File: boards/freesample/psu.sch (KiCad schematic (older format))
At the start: 117 parts, among them U26 MCP1755ST-5002E/MC, U27 LM27761, U28 ADP1763, U29 ADP1763, U30 OKL-T/3-W12P-C, U31 ADP1741, U32 OKL-T/3-W12P-C, U33 ADP1741, U34 ADP1741, U35 OKL-T/3-W12P-C, U36 OKL-T/3-W12P-C, U37 LM27761, U38 OKL-T/3-W12P-C, U39 LM27761, U42 ADP1741, U43 ADP1741

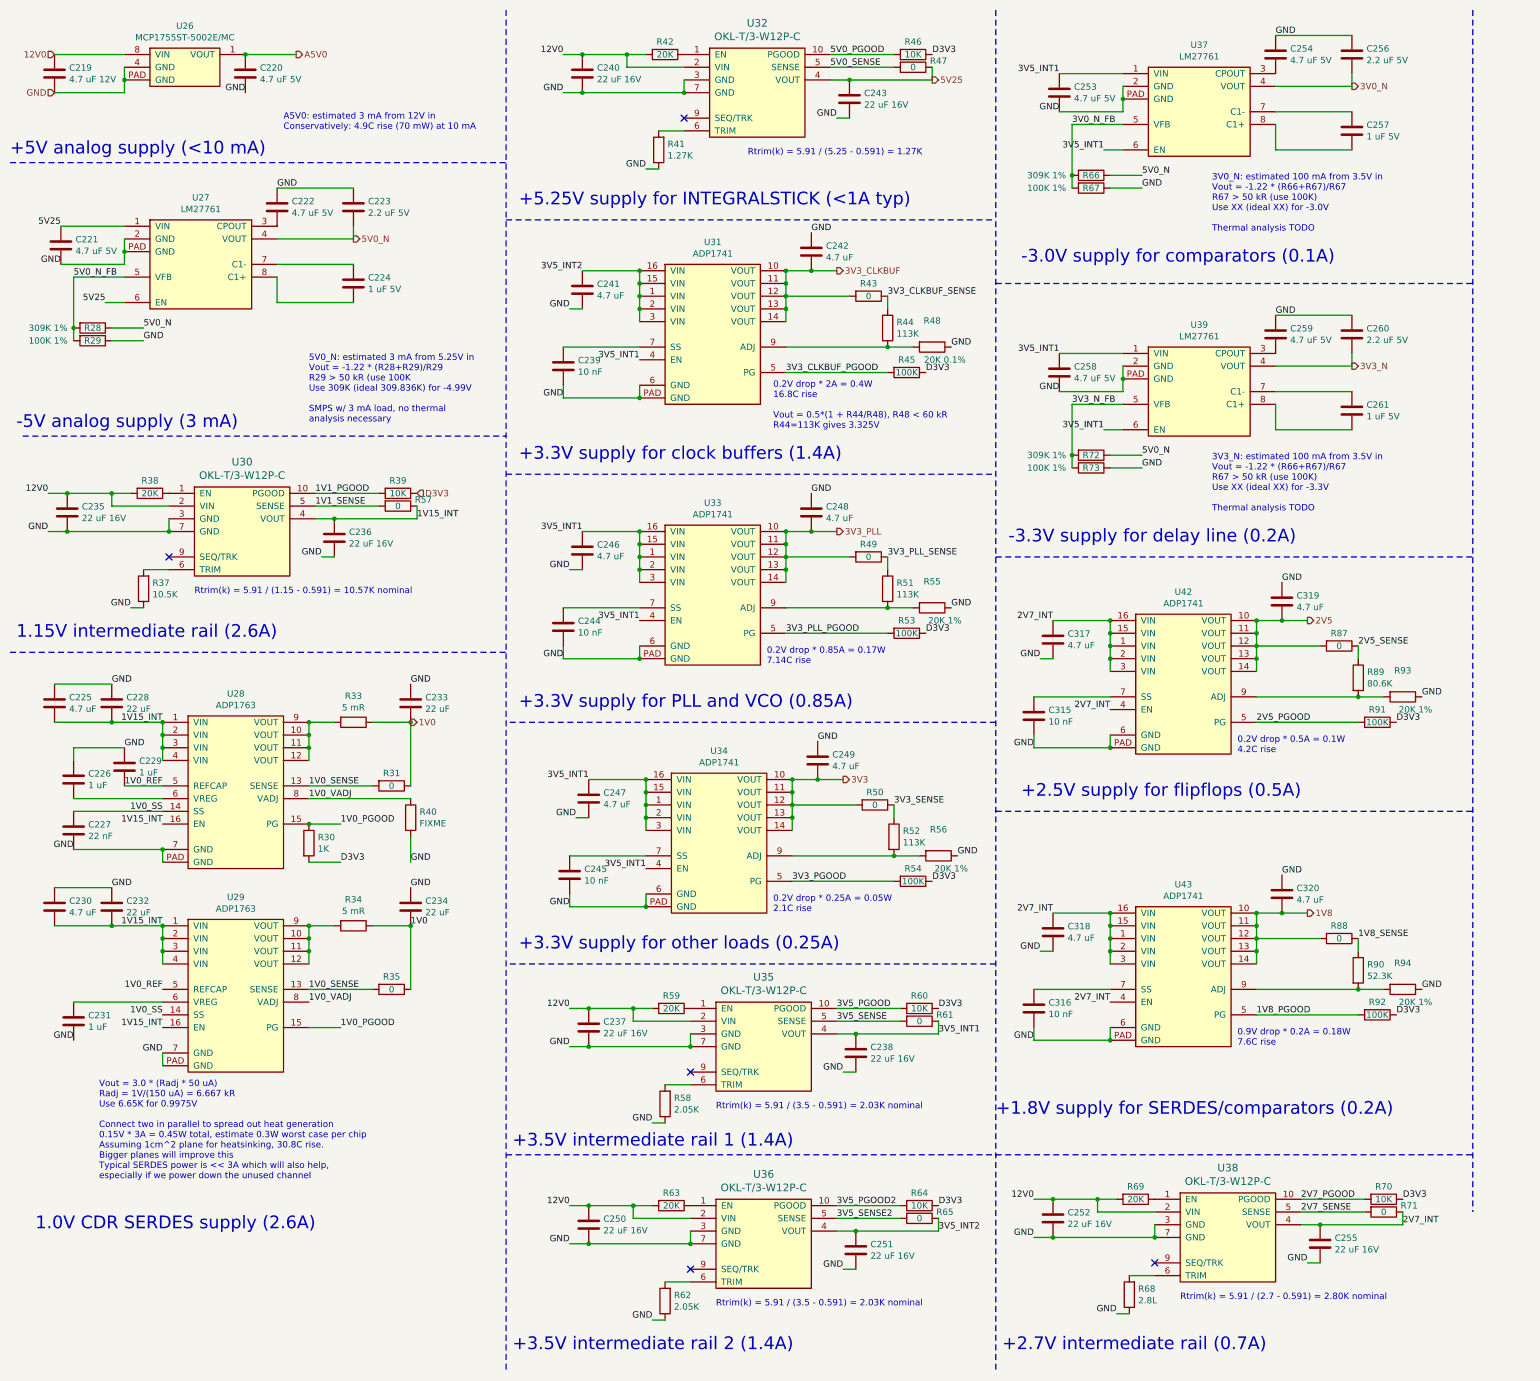
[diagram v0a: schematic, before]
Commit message: Added more test points. Started picking packages for passives. Continued schematic review.
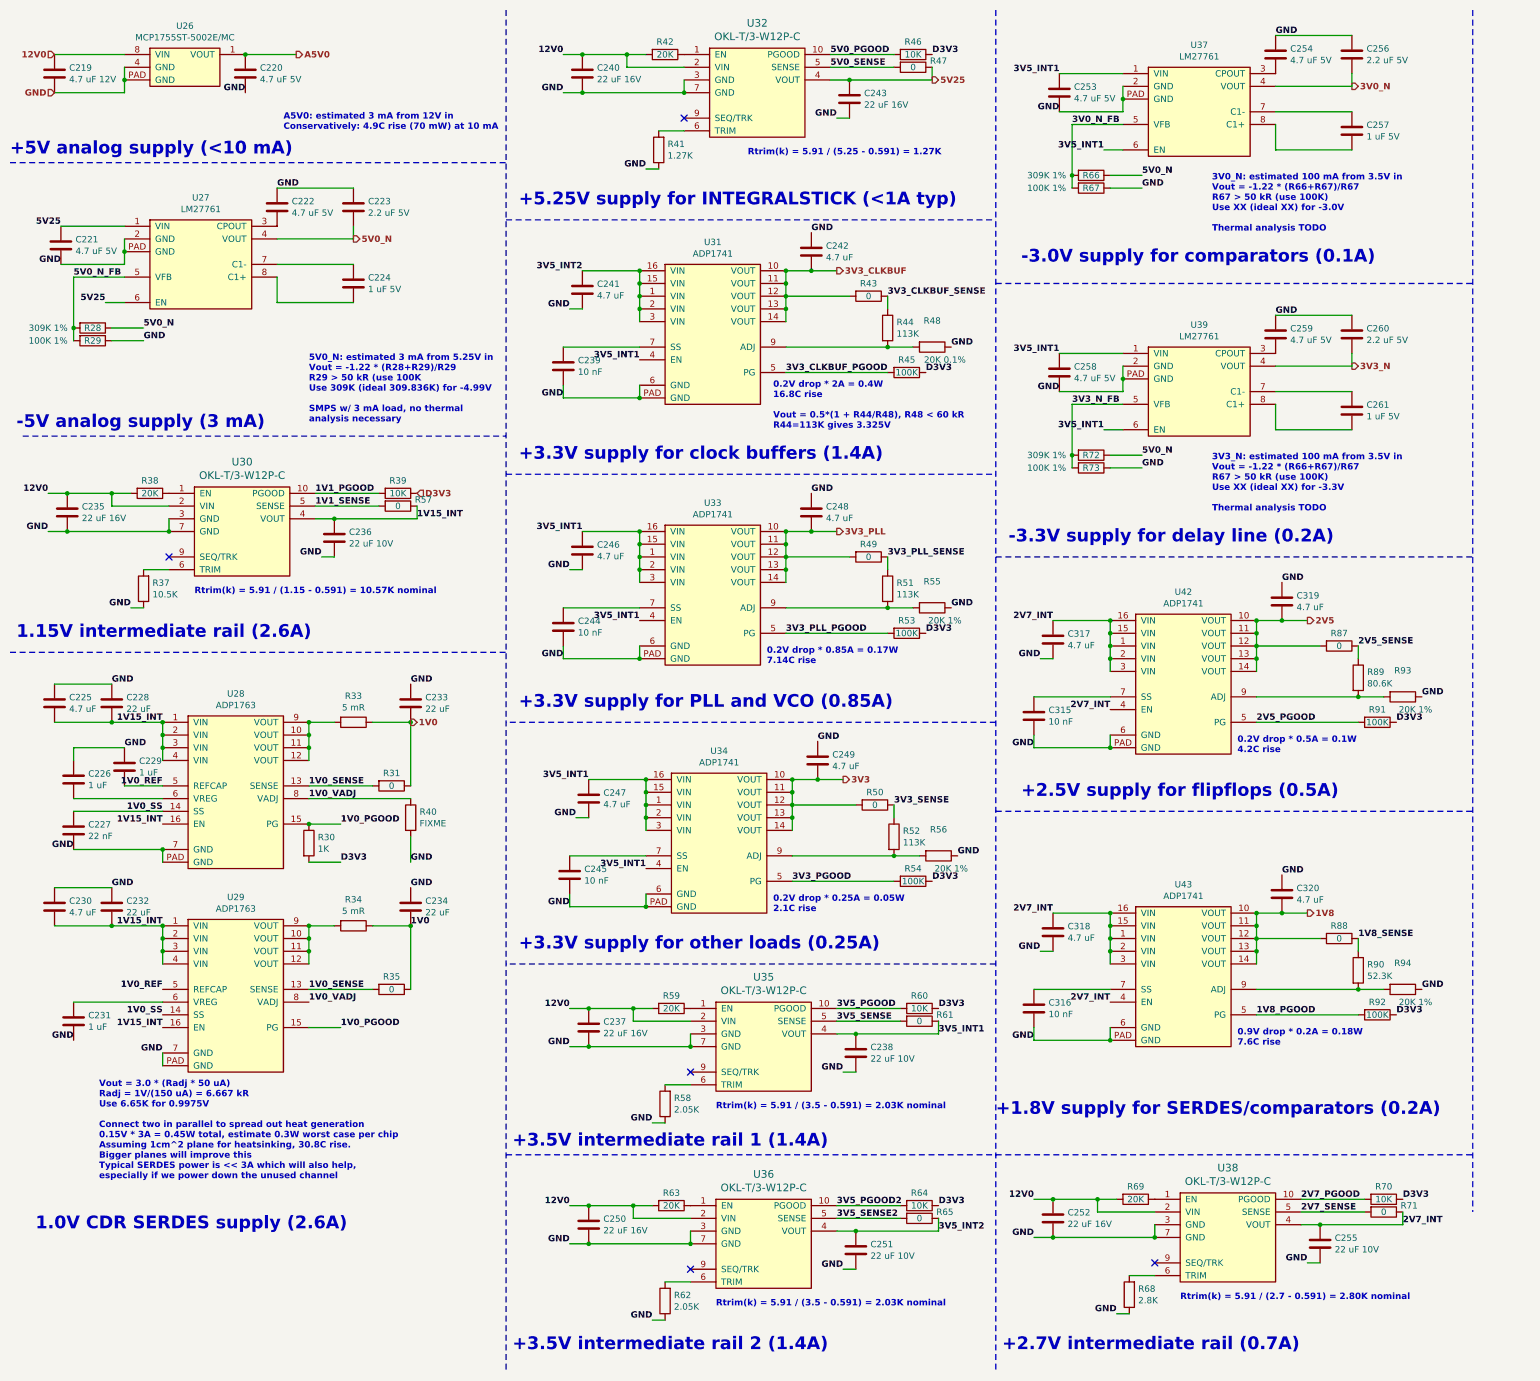
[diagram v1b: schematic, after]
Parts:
- C219, C220, C221, C222, C253, C254, C258, C259: footprint (none) -> azonenberg_pcb:EIA_1206_CAP_NOSILK
- C223, C224, C225, C226, C229, C230, C241, C242, C246, C247, C248, C249, C256, C257, C260, C261, C317, C318, C319, C320: footprint (none) -> azonenberg_pcb:EIA_0603_CAP_NOSILK
- C227, C231, C239, C244, C245, C315, C316: footprint (none) -> azonenberg_pcb:EIA_0402_CAP_NOSILK
- C228, C232, C233, C234: footprint (none) -> azonenberg_pcb:EIA_0805_CAP_NOSILK
- C235, C237, C240, C243, C250, C252: footprint (none) -> azonenberg_pcb:EIA_1812_CAP_NOSILK
- C236, C238, C251, C255: value 22 uF 16V -> 22 uF 10V; footprint (none) -> azonenberg_pcb:EIA_1210_CAP_NOSILK
- R30, R31, R35, R37, R39, R43, R45, R46, R47, R49, R50, R53, R54, R57, R61, R65, R70, R71, R87, R88, R91, R92: footprint (none) -> azonenberg_pcb:EIA_0402_RES_NOSILK
- R68: value 2.8L -> 2.8K
- U27, U37, U39: footprint (none) -> azonenberg_pcb:DFN_8_0.5MM_2x2MM
- U28, U29: footprint (none) -> azonenberg_pcb:QFN_16_0.5MM_3x3MM
- U30, U32, U35, U36, U38: footprint (none) -> azonenberg_pcb:MODULE_MURATA_OKL-T3-W12
- U31, U33, U34, U42, U43: footprint (none) -> azonenberg_pcb:QFN_16_0.65MM_4x4MM

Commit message: Continued assigning footprints
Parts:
- R28, R29, R38, R41, R42, R44, R48, R51, R52, R55, R56, R58, R59, R60, R62, R63, R64, R66, R67, R68, R69, R72, R73, R89, R90, R93, R94: footprint (none) -> azonenberg_pcb:EIA_0402_RES_NOSILK
- R33, R34: footprint (none) -> azonenberg_pcb:EIA_0603_RES_NOSILK
- R40: value FIXME -> DNP; footprint (none) -> azonenberg_pcb:EIA_0402_RES_NOSILK
- U28, U29: value ADP1763 -> ADP1763Z-1.0
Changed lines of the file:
@@
 Sheet 10 12
 Title "FREESAMPLE Oscilloscope"
-Date "2019-03-15"
+Date "2019-03-16"
 Rev "0.1"
 Comp "Andrew D. Zonenberg / Antikernel Labs"
@@
 F 0 "R28" V 1150 3000 50  0000 C CNN
 F 1 "309K 1%" V 1150 2650 50  0000 C CNN
-F 2 "" V 1080 3000 50  0001 C CNN
+F 2 "azonenberg_pcb:EIA_0402_RES_NOSILK" V 1080 3000 50  0001 C CNN
 F 3 "" H 1150 3000 50  0001 C CNN
 	1    1150 3000
@@
 F 0 "R29" V 1150 3100 50  0000 C CNN
 F 1 "100K 1%" V 1150 2750 50  0000 C CNN
-F 2 "" V 1080 3100 50  0001 C CNN
+F 2 "azonenberg_pcb:EIA_0402_RES_NOSILK" V 1080 3100 50  0001 C CNN
 F 3 "" H 1150 3100 50  0001 C CNN
 	1    1150 3100
@@
 P 1900 7250
 F 0 "U28" H 2275 8625 50  0000 C CNN
-F 1 "ADP1763" H 2275 8534 50  0000 C CNN
+F 1 "ADP1763Z-1.0" H 2275 8534 50  0000 C CNN
 F 2 "azonenberg_pcb:QFN_16_0.5MM_3x3MM" H 1900 7200 50  0001 C CNN
 F 3 "" H 1900 7200 50  0001 C CNN
@@
 F 0 "R33" V 2993 6100 50  0000 C CNN
 F 1 "5 mR" V 3084 6100 50  0000 C CNN
-F 2 "" V 3130 6100 50  0001 C CNN
+F 2 "azonenberg_pcb:EIA_0603_RES_NOSILK" V 3130 6100 50  0001 C CNN
 F 3 "" H 3200 6100 50  0001 C CNN
 	1    3200 6100
@@
 F 0 "R34" V 2993 7700 50  0000 C CNN
 F 1 "5 mR" V 3084 7700 50  0000 C CNN
-F 2 "" V 3130 7700 50  0001 C CNN
+F 2 "azonenberg_pcb:EIA_0603_RES_NOSILK" V 3130 7700 50  0001 C CNN
 F 3 "" H 3200 7700 50  0001 C CNN
 	1    3200 7700
@@
 P 1900 8850
 F 0 "U29" H 2275 10225 50  0000 C CNN
-F 1 "ADP1763" H 2275 10134 50  0000 C CNN
+F 1 "ADP1763Z-1.0" H 2275 10134 50  0000 C CNN
 F 2 "azonenberg_pcb:QFN_16_0.5MM_3x3MM" H 1900 8800 50  0001 C CNN
 F 3 "" H 1900 8800 50  0001 C CNN
@@
 F 0 "R41" H 5530 1554 50  0000 R CNN
 F 1 "1.27K" H 5530 1645 50  0000 R CNN
-F 2 "" V 5530 1600 50  0001 C CNN
+F 2 "azonenberg_pcb:EIA_0402_RES_NOSILK" V 5530 1600 50  0001 C CNN
 F 3 "" H 5600 1600 50  0001 C CNN
 	1    5600 1600
@@
 F 0 "R42" V 5550 850 50  0000 C CNN
 F 1 "20K" V 5650 850 50  0000 C CNN
-F 2 "" V 5580 850 50  0001 C CNN
+F 2 "azonenberg_pcb:EIA_0402_RES_NOSILK" V 5580 850 50  0001 C CNN
 F 3 "" H 5650 850 50  0001 C CNN
 	1    5650 850
@@
 P 3650 6850
 F 0 "R40" H 3720 6896 50  0000 L CNN
-F 1 "FIXME" H 3720 6805 50  0000 L CNN
-F 2 "" V 3580 6850 50  0001 C CNN
+F 1 "DNP" H 3720 6805 50  0000 L CNN
+F 2 "azonenberg_pcb:EIA_0402_RES_NOSILK" V 3580 6850 50  0001 C CNN
 F 3 "" H 3650 6850 50  0001 C CNN
 	1    3650 6850
@@
 F 0 "R44" H 7470 3046 50  0000 L CNN
 F 1 "113K" H 7470 2955 50  0000 L CNN
-F 2 "" V 7330 3000 50  0001 C CNN
+F 2 "azonenberg_pcb:EIA_0402_RES_NOSILK" V 7330 3000 50  0001 C CNN
 F 3 "" H 7400 3000 50  0001 C CNN
 	1    7400 3000
@@
 F 0 "R48" V 7543 3150 50  0000 C CNN
 F 1 "20K 0.1%" V 7850 3250 50  0000 C CNN
-F 2 "" V 7680 3150 50  0001 C CNN
+F 2 "azonenberg_pcb:EIA_0402_RES_NOSILK" V 7680 3150 50  0001 C CNN
 F 3 "" H 7750 3150 50  0001 C CNN
 	1    7750 3150
@@
 F 0 "R51" H 7470 5096 50  0000 L CNN
 F 1 "113K" H 7470 5005 50  0000 L CNN
-F 2 "" V 7330 5050 50  0001 C CNN
+F 2 "azonenberg_pcb:EIA_0402_RES_NOSILK" V 7330 5050 50  0001 C CNN
 F 3 "" H 7400 5050 50  0001 C CNN
 	1    7400 5050
@@
 F 0 "R55" V 7543 5200 50  0000 C CNN
 F 1 "20K 1%" V 7850 5300 50  0000 C CNN
-F 2 "" V 7680 5200 50  0001 C CNN
+F 2 "azonenberg_pcb:EIA_0402_RES_NOSILK" V 7680 5200 50  0001 C CNN
 F 3 "" H 7750 5200 50  0001 C CNN
 	1    7750 5200
@@
 F 0 "R52" H 7520 7046 50  0000 L CNN
 F 1 "113K" H 7520 6955 50  0000 L CNN
-F 2 "" V 7380 7000 50  0001 C CNN
+F 2 "azonenberg_pcb:EIA_0402_RES_NOSILK" V 7380 7000 50  0001 C CNN
 F 3 "" H 7450 7000 50  0001 C CNN
 	1    7450 7000
@@
 F 0 "R56" V 7593 7150 50  0000 C CNN
 F 1 "20K 1%" V 7900 7250 50  0000 C CNN
-F 2 "" V 7730 7150 50  0001 C CNN
+F 2 "azonenberg_pcb:EIA_0402_RES_NOSILK" V 7730 7150 50  0001 C CNN
 F 3 "" H 7800 7150 50  0001 C CNN
 	1    7800 7150
@@
 F 0 "R58" H 5580 9054 50  0000 R CNN
 F 1 "2.05K" H 5580 9145 50  0000 R CNN
-F 2 "" V 5580 9100 50  0001 C CNN
+F 2 "azonenberg_pcb:EIA_0402_RES_NOSILK" V 5580 9100 50  0001 C CNN
 F 3 "" H 5650 9100 50  0001 C CNN
 	1    5650 9100
@@
 F 0 "R60" V 7550 8350 50  0000 C CNN
 F 1 "10K" V 7650 8350 50  0000 C CNN
-F 2 "" V 7580 8350 50  0001 C CNN
+F 2 "azonenberg_pcb:EIA_0402_RES_NOSILK" V 7580 8350 50  0001 C CNN
 F 3 "" H 7650 8350 50  0001 C CNN
 	1    7650 8350
@@
 F 0 "R59" V 5600 8350 50  0000 C CNN
 F 1 "20K" V 5700 8350 50  0000 C CNN
-F 2 "" V 5630 8350 50  0001 C CNN
+F 2 "azonenberg_pcb:EIA_0402_RES_NOSILK" V 5630 8350 50  0001 C CNN
 F 3 "" H 5700 8350 50  0001 C CNN
 	1    5700 8350
@@
 F 0 "R38" V 1500 4300 50  0000 C CNN
 F 1 "20K" V 1600 4300 50  0000 C CNN
-F 2 "" V 1530 4300 50  0001 C CNN
+F 2 "azonenberg_pcb:EIA_0402_RES_NOSILK" V 1530 4300 50  0001 C CNN
 F 3 "" H 1600 4300 50  0001 C CNN
 	1    1600 4300
@@
 F 0 "R68" H 9230 10554 50  0000 R CNN
 F 1 "2.8K" H 9230 10645 50  0000 R CNN
-F 2 "" V 9230 10600 50  0001 C CNN
+F 2 "azonenberg_pcb:EIA_0402_RES_NOSILK" V 9230 10600 50  0001 C CNN
 F 3 "" H 9300 10600 50  0001 C CNN
 	1    9300 10600
@@
 F 0 "R69" V 9250 9850 50  0000 C CNN
 F 1 "20K" V 9350 9850 50  0000 C CNN
-F 2 "" V 9280 9850 50  0001 C CNN
+F 2 "azonenberg_pcb:EIA_0402_RES_NOSILK" V 9280 9850 50  0001 C CNN
 F 3 "" H 9350 9850 50  0001 C CNN
 	1    9350 9850
@@
 F 0 "R62" H 5580 10604 50  0000 R CNN
 F 1 "2.05K" H 5580 10695 50  0000 R CNN
-F 2 "" V 5580 10650 50  0001 C CNN
+F 2 "azonenberg_pcb:EIA_0402_RES_NOSILK" V 5580 10650 50  0001 C CNN
 F 3 "" H 5650 10650 50  0001 C CNN
 	1    5650 10650
@@
 F 0 "R64" V 7550 9900 50  0000 C CNN
 F 1 "10K" V 7650 9900 50  0000 C CNN
-F 2 "" V 7580 9900 50  0001 C CNN
+F 2 "azonenberg_pcb:EIA_0402_RES_NOSILK" V 7580 9900 50  0001 C CNN
 F 3 "" H 7650 9900 50  0001 C CNN
 	1    7650 9900
@@
 F 0 "R63" V 5600 9900 50  0000 C CNN
 F 1 "20K" V 5700 9900 50  0000 C CNN
-F 2 "" V 5630 9900 50  0001 C CNN
+F 2 "azonenberg_pcb:EIA_0402_RES_NOSILK" V 5630 9900 50  0001 C CNN
 F 3 "" H 5700 9900 50  0001 C CNN
 	1    5700 9900
@@
 F 0 "R66" V 9000 1800 50  0000 C CNN
 F 1 "309K 1%" V 9000 1450 50  0000 C CNN
-F 2 "" V 8930 1800 50  0001 C CNN
+F 2 "azonenberg_pcb:EIA_0402_RES_NOSILK" V 8930 1800 50  0001 C CNN
 F 3 "" H 9000 1800 50  0001 C CNN
 	1    9000 1800
@@
 F 0 "R67" V 9000 1900 50  0000 C CNN
 F 1 "100K 1%" V 9000 1550 50  0000 C CNN
-F 2 "" V 8930 1900 50  0001 C CNN
+F 2 "azonenberg_pcb:EIA_0402_RES_NOSILK" V 8930 1900 50  0001 C CNN
 F 3 "" H 9000 1900 50  0001 C CNN
 	1    9000 1900
@@
 F 0 "R72" V 9000 4000 50  0000 C CNN
 F 1 "309K 1%" V 9000 3650 50  0000 C CNN
-F 2 "" V 8930 4000 50  0001 C CNN
+F 2 "azonenberg_pcb:EIA_0402_RES_NOSILK" V 8930 4000 50  0001 C CNN
 F 3 "" H 9000 4000 50  0001 C CNN
 	1    9000 4000
@@
 F 0 "R73" V 9000 4100 50  0000 C CNN
 F 1 "100K 1%" V 9000 3750 50  0000 C CNN
-F 2 "" V 8930 4100 50  0001 C CNN
+F 2 "azonenberg_pcb:EIA_0402_RES_NOSILK" V 8930 4100 50  0001 C CNN
 F 3 "" H 9000 4100 50  0001 C CNN
 	1    9000 4100
@@
 F 0 "R89" H 11170 5796 50  0000 L CNN
 F 1 "80.6K" H 11170 5705 50  0000 L CNN
-F 2 "" V 11030 5750 50  0001 C CNN
+F 2 "azonenberg_pcb:EIA_0402_RES_NOSILK" V 11030 5750 50  0001 C CNN
 F 3 "" H 11100 5750 50  0001 C CNN
 	1    11100 5750
@@
 F 0 "R93" V 11243 5900 50  0000 C CNN
 F 1 "20K 1%" V 11550 6000 50  0000 C CNN
-F 2 "" V 11380 5900 50  0001 C CNN
+F 2 "azonenberg_pcb:EIA_0402_RES_NOSILK" V 11380 5900 50  0001 C CNN
 F 3 "" H 11450 5900 50  0001 C CNN
 	1    11450 5900
@@
 F 0 "R90" H 11170 8096 50  0000 L CNN
 F 1 "52.3K" H 11170 8005 50  0000 L CNN
-F 2 "" V 11030 8050 50  0001 C CNN
+F 2 "azonenberg_pcb:EIA_0402_RES_NOSILK" V 11030 8050 50  0001 C CNN
 F 3 "" H 11100 8050 50  0001 C CNN
 	1    11100 8050
@@
 F 0 "R94" V 11243 8200 50  0000 C CNN
 F 1 "20K 1%" V 11550 8300 50  0000 C CNN
-F 2 "" V 11380 8200 50  0001 C CNN
+F 2 "azonenberg_pcb:EIA_0402_RES_NOSILK" V 11380 8200 50  0001 C CNN
 F 3 "" H 11450 8200 50  0001 C CNN
 	1    11450 8200

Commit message: Continued selecting component footprints and working on schematic review
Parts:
- U26: footprint (none) -> azonenberg_pcb:DFN_8_0.5MM_3x3MM
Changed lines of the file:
@@
 F 0 "U26" H 1875 1575 50  0000 C CNN
 F 1 "MCP1755ST-5002E/MC" H 1875 1484 50  0000 C CNN
-F 2 "" H 1600 1100 50  0001 C CNN
+F 2 "azonenberg_pcb:DFN_8_0.5MM_3x3MM" H 1600 1100 50  0001 C CNN
 F 3 "" H 1600 1100 50  0001 C CNN
 	1    1600 1100
